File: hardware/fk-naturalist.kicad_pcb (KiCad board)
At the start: 2 copper layers, 106 x 37 mm, 140 parts, among them J1 Conn_01x11, J10 S2B-PH-SM4-TB, J11 RF-SMA-EDGE, J2 Conn_01x05, J3 Conn_01x04, J5 Conn_01x03, J6 Conn_01x05, J7 CONN-HDR-2x5, J8 Conn_01x09, J9 MICRO-USB, M1 MOUNT_HOLE, M3 MOUNT_HOLE, M4 MOUNT_HOLE, M6 MOUNT_HOLE, M7 MICROSD, Q1 2N7002LT1G, Q2 2N7002LT1G, Q3 2N7002LT1G, Q4 2N7002LT1G, SW1 SPNO, SW2 SPNO, U1 ATWINC1500-MR210PA, U10 FGPMMOPA6H, U101 TSL2591, U102 MPL3115A2, U103 BNO055, U104 SHT31, U11 MAX1704XX, U2 ATSAMD21G18A-AU, U3 SPH0645, U4 24AA02E64, U5 S25FL116K0XMFI041, U6 BQ24074RGTT, U7 PCF8523, U8 MCP1700T-3302E/MB, U9 ISL8541x, Y1 FC-135, Y101 FC-135, Y2 FC-135

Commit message: Bump revision.
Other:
- board text added: "v0.8"
- board text removed: "v0.7"
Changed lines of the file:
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@@
     (effects (font (size 1 1) (thickness 0.2)))
   )
-  (gr_text v0.7 (at 82.6008 110.6932 180) (layer F.SilkS)
+  (gr_text v0.8 (at 82.6008 110.6932 180) (layer F.SilkS)
     (effects (font (size 1 1) (thickness 0.2)))
   )

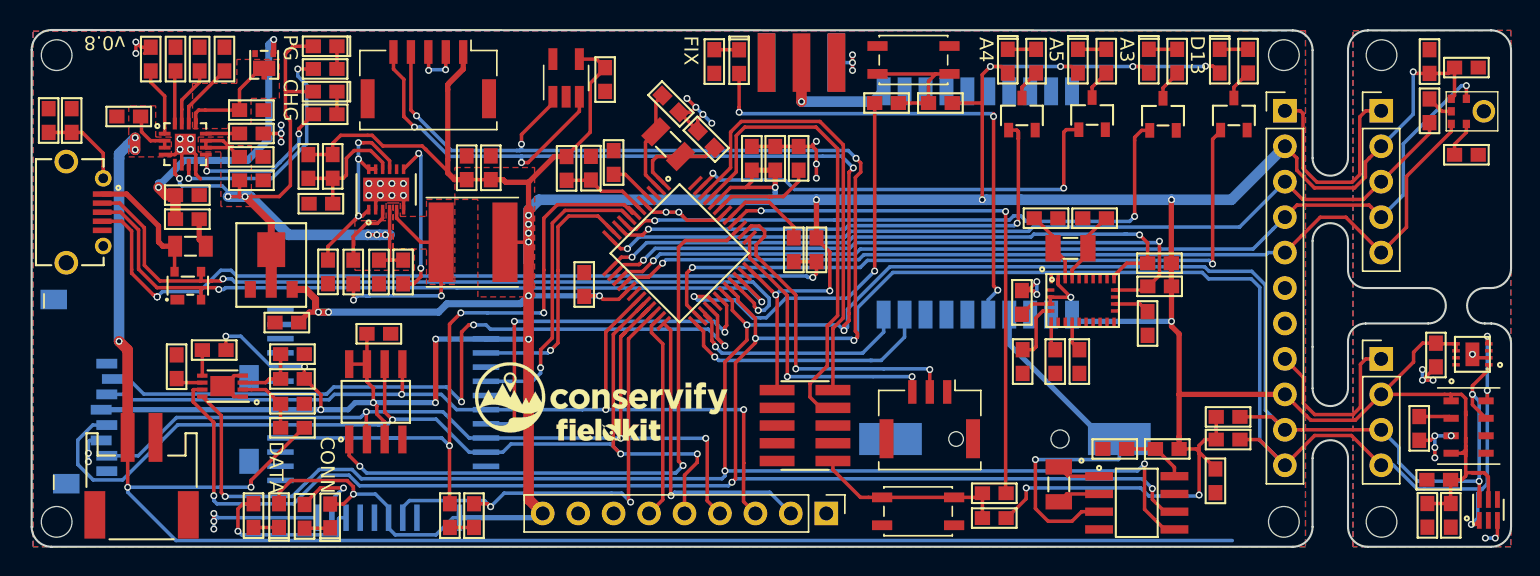
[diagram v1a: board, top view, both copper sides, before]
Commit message: Adding peripheral enable NFET.
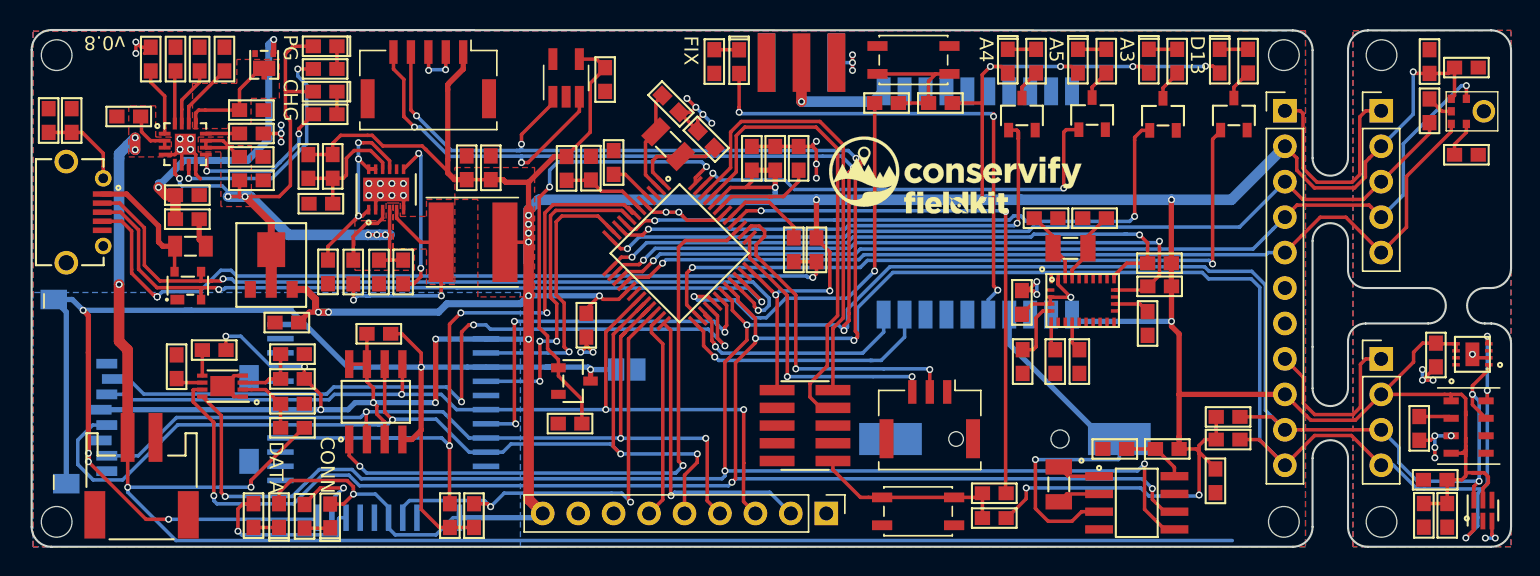
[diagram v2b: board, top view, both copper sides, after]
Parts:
- added J4: Conn_01x02, conservify:SJ_OPEN, B.Cu at (120.0, 134.1)
- added Q5: 2N7002LT1G, RocketScreamKicadLibrary:SOT-23, F.Cu at (116.3, 134.9)
- added R6: 10K, RocketScreamKicadLibrary:RES-0603, F.Cu at (116.0, 138.0)
- moved G*** 30.1 mm to (143.6, 119.9)
- moved G*** 29.8 mm to (143.6, 122.1)
- moved C5 2.92 mm to (117.1, 130.9), turned to 270 degrees
- moved U101 0.39 mm to (181.4, 144.2)
- moved C101 0.25 mm to (178.0, 142.0)
- moved C103 0.25 mm to (178.8, 144.6)
- moved C104 0.25 mm to (177.1, 144.6)
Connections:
- C18 pad 2: GND -> /PERIPH_GND
- M7 pad 6: GND -> /PERIPH_GND
- M7 pad MT1: GND -> /PERIPH_GND
- M7 pad MT2: GND -> /PERIPH_GND
- R1 pad 2: GND -> /PERIPH_GND
- R2 pad 2: GND -> /PERIPH_GND
- U1 pad 12: GND -> /PERIPH_GND
- U1 pad 28: GND -> /PERIPH_GND
- U1 pad 9: GND -> /PERIPH_GND
- U2 pad 48: Net-(U2-Pad48) -> /PERIPH_ENABLE
- U5 pad 4: GND -> /PERIPH_GND
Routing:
- net /PERIPH_GND: track 0.00 -> 108.8 mm, vias 0 -> 6
- net /PERIPH_ENABLE: track 0.00 -> 32.9 mm, vias 0 -> 2
- net GND: track 104.3 -> 94.0 mm, vias 48 -> 45
- net /WIFI_WAKE: track 19.4 -> 21.3 mm
- net /SCL: track 242.9 -> 244.8 mm
- net /WIFI_IRQ: track 22.1 -> 23.9 mm, vias 1 -> 3
- net 3V3: track 436.7 -> 437.7 mm
- added copper zone on B.Cu, net /PERIPH_GND

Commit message: Fix stencil on audio chip and plotting.
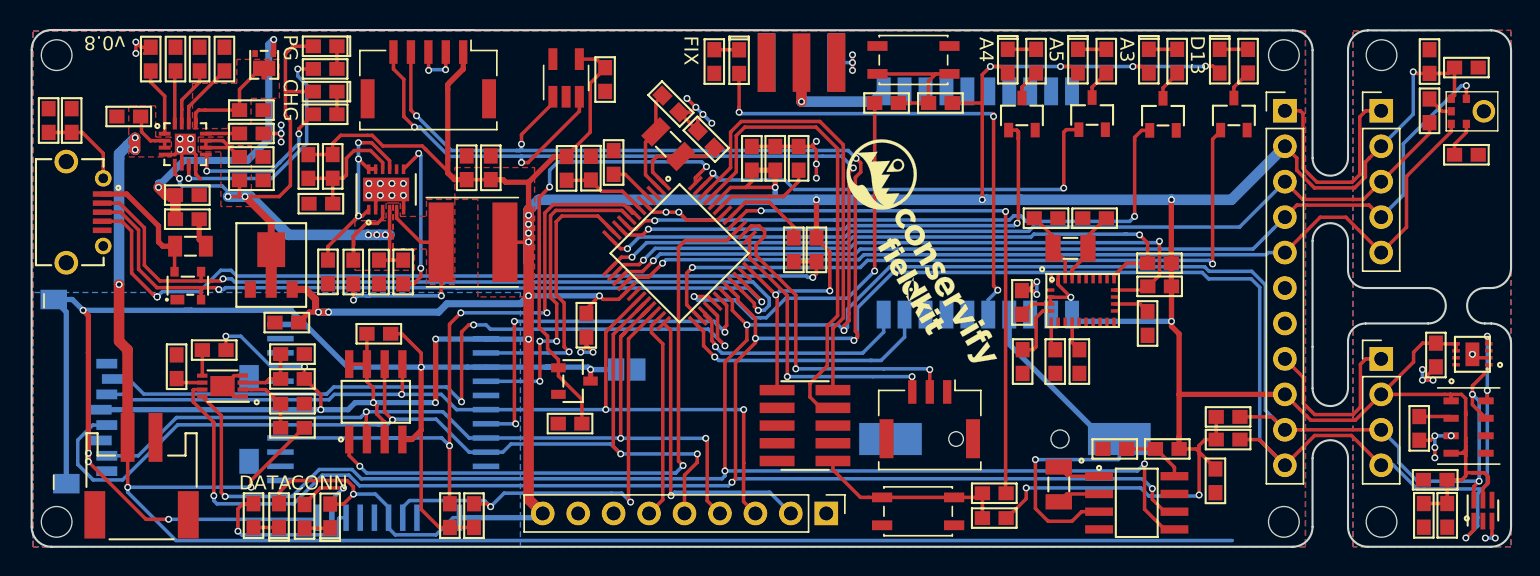
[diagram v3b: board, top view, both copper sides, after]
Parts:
- moved G*** 6.72 mm to (140.5, 128.1), turned to 300 degrees
- moved G*** 6.19 mm to (141.5, 125.8), turned to 300 degrees
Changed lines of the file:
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@@
     (37 F.SilkS user)
     (38 B.Mask user)
-    (39 F.Mask user)
+    (39 F.Mask user hide)
     (40 Dwgs.User user)
     (41 Cmts.User user hide)
@@
   )
   (module conservify:fk_negative_2500 (layer F.Cu)
-    (at 143.6116 122.1486)
-    (fp_text reference G*** (at 0 0) (layer F.SilkS) hide
+    (at 140.462 128.0795 300)
+    (fp_text reference G*** (at 0 0 300) (layer F.SilkS) hide
       (effects (font (thickness 0.3)))
     )
-    (fp_text value LOGO (at 0.75 0) (layer F.SilkS) hide
+    (fp_text value LOGO (at 0.75 0 300) (layer F.SilkS) hide
       (effects (font (thickness 0.3)))
     )
@@
   )
   (module conservify:conservify_text_negative_4000 (layer F.Cu)
-    (at 143.5608 119.9388)
-    (fp_text reference G*** (at 0 0) (layer F.SilkS) hide
+    (at 141.5415 125.7935 300)
+    (fp_text reference G*** (at 0 0 300) (layer F.SilkS) hide
       (effects (font (thickness 0.3)))
     )
-    (fp_text value LOGO (at 0.75 0) (layer F.SilkS) hide
+    (fp_text value LOGO (at 0.75 0 300) (layer F.SilkS) hide
       (effects (font (thickness 0.3)))
     )
@@
     (pad 4 smd rect (at 3.35 2.8) (size 1.5 3.4) (layers F.Cu F.Paste F.Mask)
       (net 84 "Net-(J10-Pad4)"))
-    (model Connectors_JST.3dshapes/JST_PH_S2B-PH-K_02x2.00mm_Angled.wrl
-      (at (xyz -0.05 0.05 0))
-      (scale (xyz 1 1 1))
-      (rotate (xyz 0 0 0))
-    )
   )
   (module RocketScreamKicadLibrary:RF-SMA-EDGE (layer F.Cu)
@@
     )
   )
-  (module conservify:SPH0645LM4H-B (layer F.Cu)
-    (at 181.4396 115.6064 90)
-    (fp_text reference U3 (at 0 -3.302 90) (layer F.SilkS) hide
-      (effects (font (size 1 1) (thickness 0.15)))
-    )
-    (fp_text value SPH0645 (at 0 1.8 90) (layer F.Fab)
-      (effects (font (size 1 1) (thickness 0.15)))
-    )
-    (fp_line (start -1.4 1) (end 1.4 1) (layer F.SilkS) (width 0.1))
-    (fp_line (start 1.4 1) (end 1.4 -2.7) (layer F.SilkS) (width 0.1))
-    (fp_line (start 1.4 -2.7) (end -1.4 -2.7) (layer F.SilkS) (width 0.1))
-    (fp_line (start -1.4 -2.7) (end -1.4 1) (layer F.SilkS) (width 0.1))
-    (pad 4 smd rect (at 0.9 -1.252 90) (size 0.6 0.522) (layers F.Cu F.Paste F.Mask)
-      (net 122 /I2S_BCLK))
-    (pad 5 smd rect (at 0.9 -2.335 90) (size 0.6 0.522) (layers F.Cu F.Paste F.Mask)
-      (net 2 3V3))
-    (pad 2 smd rect (at -0.9 -1.252 90) (size 0.6 0.522) (layers F.Cu F.Paste F.Mask)
-      (net 97 "Net-(R11-Pad2)"))
-    (pad 1 smd rect (at -0.9 -2.335 90) (size 0.6 0.522) (layers F.Cu F.Paste F.Mask)
-      (net 123 /I2S_WS))
-    (pad 3 thru_hole circle (at 0 0 90) (size 1.624 1.624) (drill 1.024) (layers *.Cu *.Mask F.SilkS)
-      (net 1 GND))
-    (pad 6 smd rect (at 0 -2.335 90) (size 0.6 0.522) (layers F.Cu F.Paste F.Mask)
-      (net 98 "Net-(R12-Pad1)"))
-  )
   (module TO_SOT_Packages_SMD:SOT-23-5_HandSoldering (layer F.Cu)
     (at 115.671358 113.213792 90)
@@
       (net 1 GND))
   )
+  (module conservify:SPH0645LM4H-B (layer F.Cu)
+    (at 181.4396 115.6064 90)
+    (fp_text reference U3 (at 0 -3.302 90) (layer F.SilkS) hide
+      (effects (font (size 1 1) (thickness 0.15)))
+    )
+    (fp_text value SPH0645 (at 0 1.8 90) (layer F.Fab)
+      (effects (font (size 1 1) (thickness 0.15)))
+    )
+    (fp_line (start -1.4 1) (end 1.4 1) (layer F.SilkS) (width 0.1))
+    (fp_line (start 1.4 1) (end 1.4 -2.7) (layer F.SilkS) (width 0.1))
+    (fp_line (start 1.4 -2.7) (end -1.4 -2.7) (layer F.SilkS) (width 0.1))
+    (fp_line (start -1.4 -2.7) (end -1.4 1) (layer F.SilkS) (width 0.1))
+    (pad 4 smd rect (at 0.9 -1.252 90) (size 0.6 0.522) (layers F.Cu F.Paste F.Mask)
+      (net 122 /I2S_BCLK))
+    (pad 5 smd rect (at 0.9 -2.335 90) (size 0.6 0.522) (layers F.Cu F.Paste F.Mask)
+      (net 2 3V3))
+    (pad 2 smd rect (at -0.9 -1.252 90) (size 0.6 0.522) (layers F.Cu F.Paste F.Mask)
+      (net 97 "Net-(R11-Pad2)"))
+    (pad 1 smd rect (at -0.9 -2.335 90) (size 0.6 0.522) (layers F.Cu F.Paste F.Mask)
+      (net 123 /I2S_WS))
+    (pad 3 thru_hole circle (at 0 0 90) (size 1.624 1.624) (drill 1.024) (layers *.Cu *.Mask F.Paste F.SilkS)
+      (net 1 GND))
+    (pad 6 smd rect (at 0 -2.335 90) (size 0.6 0.522) (layers F.Cu F.Paste F.Mask)
+      (net 98 "Net-(R12-Pad1)"))
+  )
   (gr_circle (center 182.6006 133.77631) (end 182.5506 133.72631) (layer F.SilkS) (width 0.3))
   (gr_circle (center 179.1208 134.9502) (end 179.0708 134.9002) (layer F.SilkS) (width 0.3))
@@
   (gr_circle (center 152.6032 140.6398) (end 152.5532 140.5898) (layer F.SilkS) (width 0.3))
   (gr_circle (center 149.7838 126.9238) (end 149.7338 126.8738) (layer F.SilkS) (width 0.3))
-  (gr_text DATA (at 94.8817 141.1351 270) (layer F.SilkS)
+  (gr_text DATA (at 94.107 142.24 360) (layer F.SilkS)
     (effects (font (size 1 1) (thickness 0.2)))
   )
-  (gr_text CONN (at 98.552 140.9573 270) (layer F.SilkS)
+  (gr_text CONN (at 97.9805 142.24 360) (layer F.SilkS)
     (effects (font (size 1 1) (thickness 0.2)))
   )

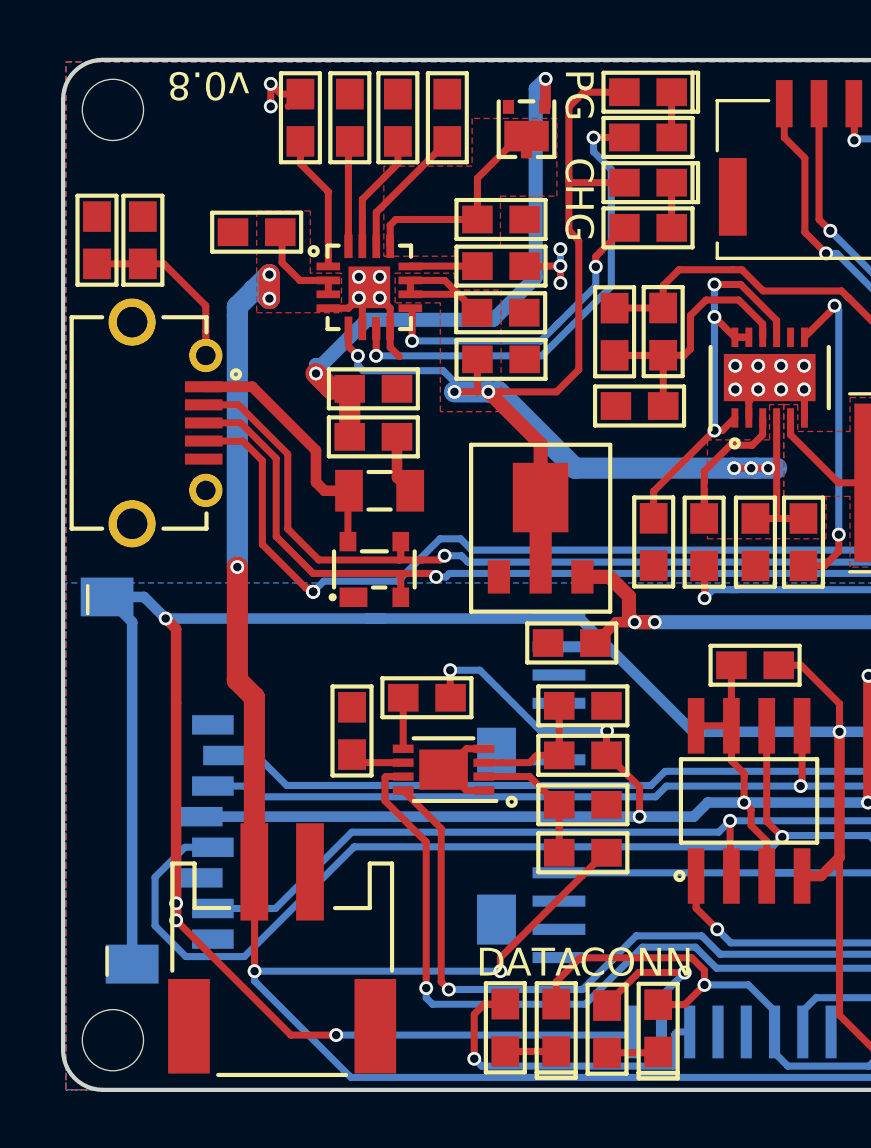
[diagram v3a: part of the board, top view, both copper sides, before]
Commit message: Widen gap between USB and SD. Nudge USB out.
Giovanni recommended we make these changes to ease our enclosure design.
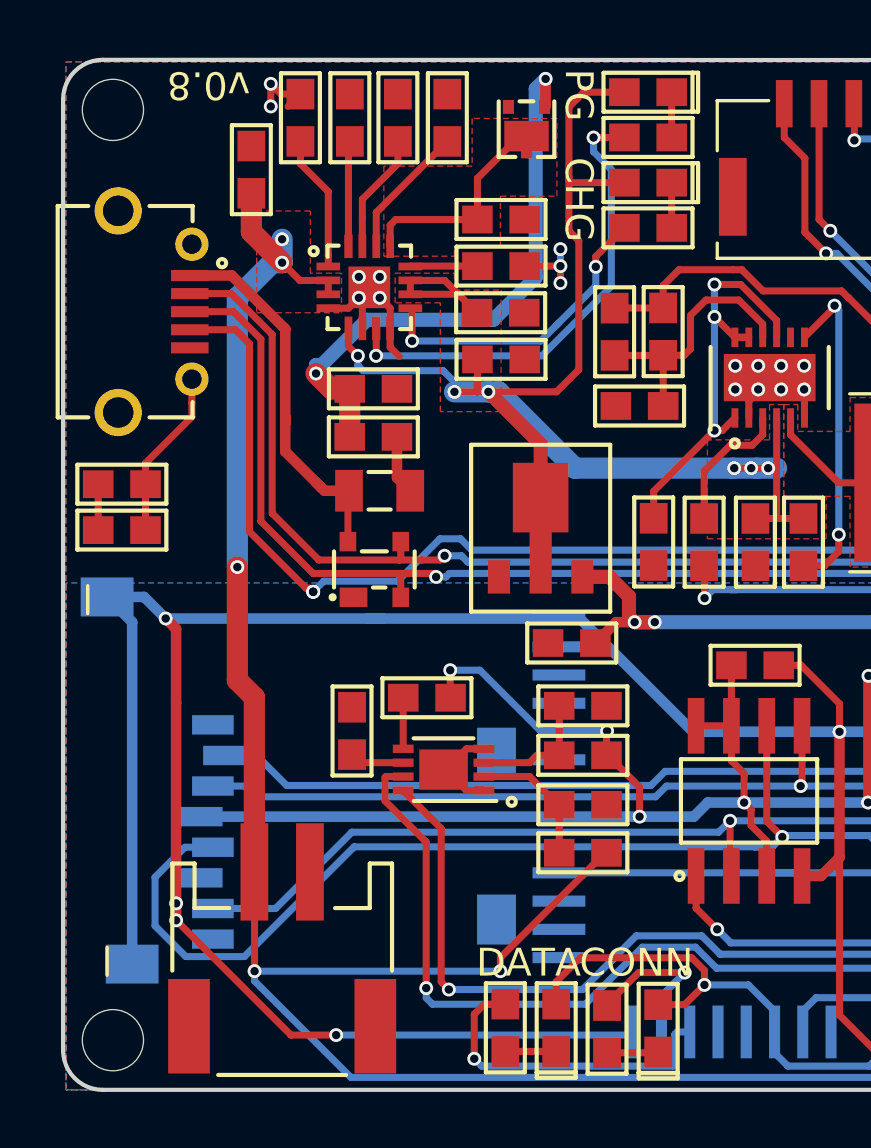
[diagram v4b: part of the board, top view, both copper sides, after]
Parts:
- moved R31 10.5 mm to (79.5, 126.7), turned to 180 degrees
- moved C14 8.80 mm to (79.5, 125.0), turned to 180 degrees
- moved J9 4.03 mm to (80.5, 118.8)
- moved C19 2.26 mm to (84.1, 113.7), turned to 90 degrees
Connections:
- J9 pad 6: Net-(C14-Pad1) -> Net-(J9-Pad6)
- J9 pad 7: Net-(J9-Pad7) -> Net-(C14-Pad1)
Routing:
- net VUSB: track 9.28 -> 13.9 mm
- net Net-(J9-Pad4): track 58.8 -> 63.1 mm
- net /USB+: track 54.8 -> 59.2 mm
- net /USB-: track 57.0 -> 61.4 mm
- net VBAT: track 126.2 -> 128.5 mm
- net GND: track 94.0 -> 95.6 mm
